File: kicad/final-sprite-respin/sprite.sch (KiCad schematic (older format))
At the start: 69 parts, among them J1 M20-7910442R, U1 CC430F513X, U2 LSM9DS1, U3 SPRITETCXO_TCXO_7Z, U4 DRV8837, U5 ADP5092, U6 DRV8837, U7 DRV8837, U8 TASC, U9 TASC, X1 SPRITEPIN_SPRITE_PIN, X2 SPRITEPIN_SPRITE_PIN

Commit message: Route spiral inductor
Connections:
- net labels added: SPIRAL
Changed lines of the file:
@@
 Wire Wire Line
 	15250 2950 15950 2950
+Text Label 8350 8950 0    50   ~ 0
+SPIRAL
 $EndSCHEMATC

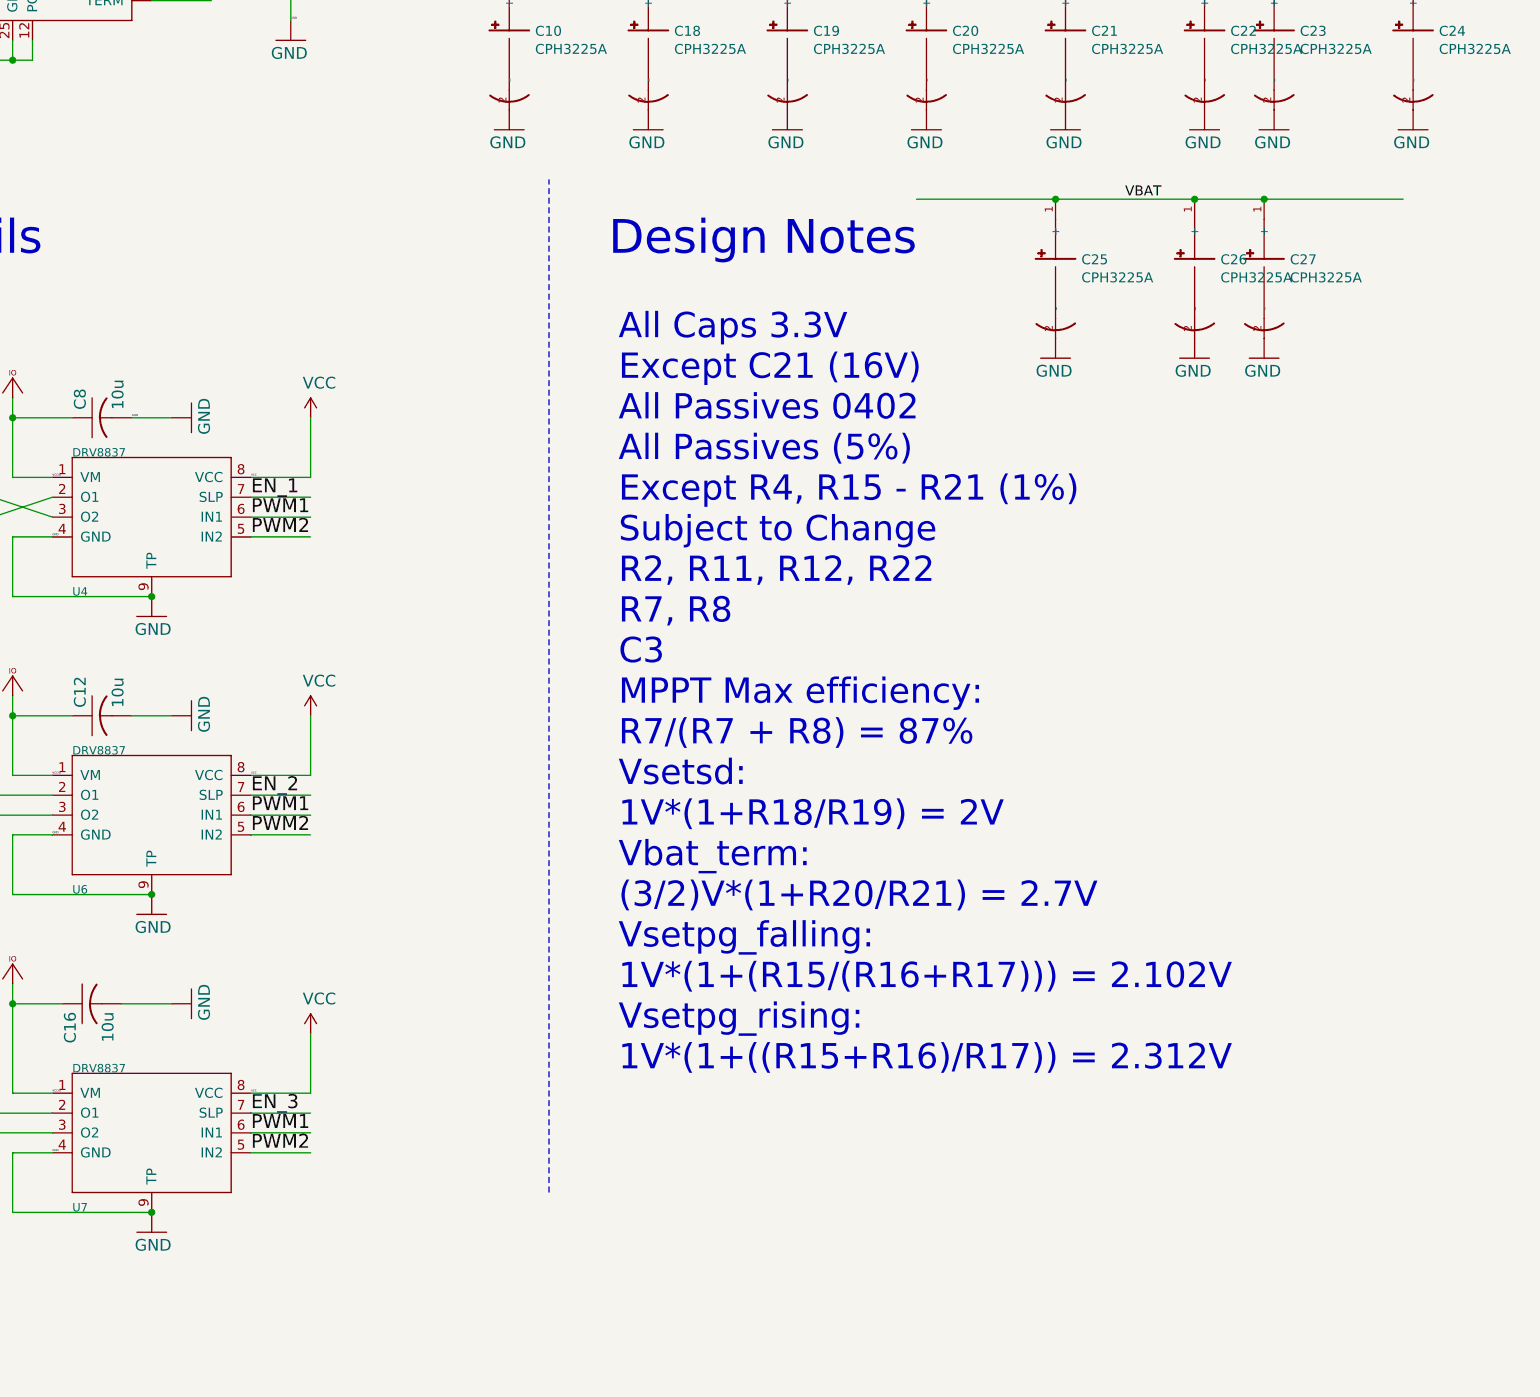
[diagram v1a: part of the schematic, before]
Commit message: updated pcb with spots for 6 more caps
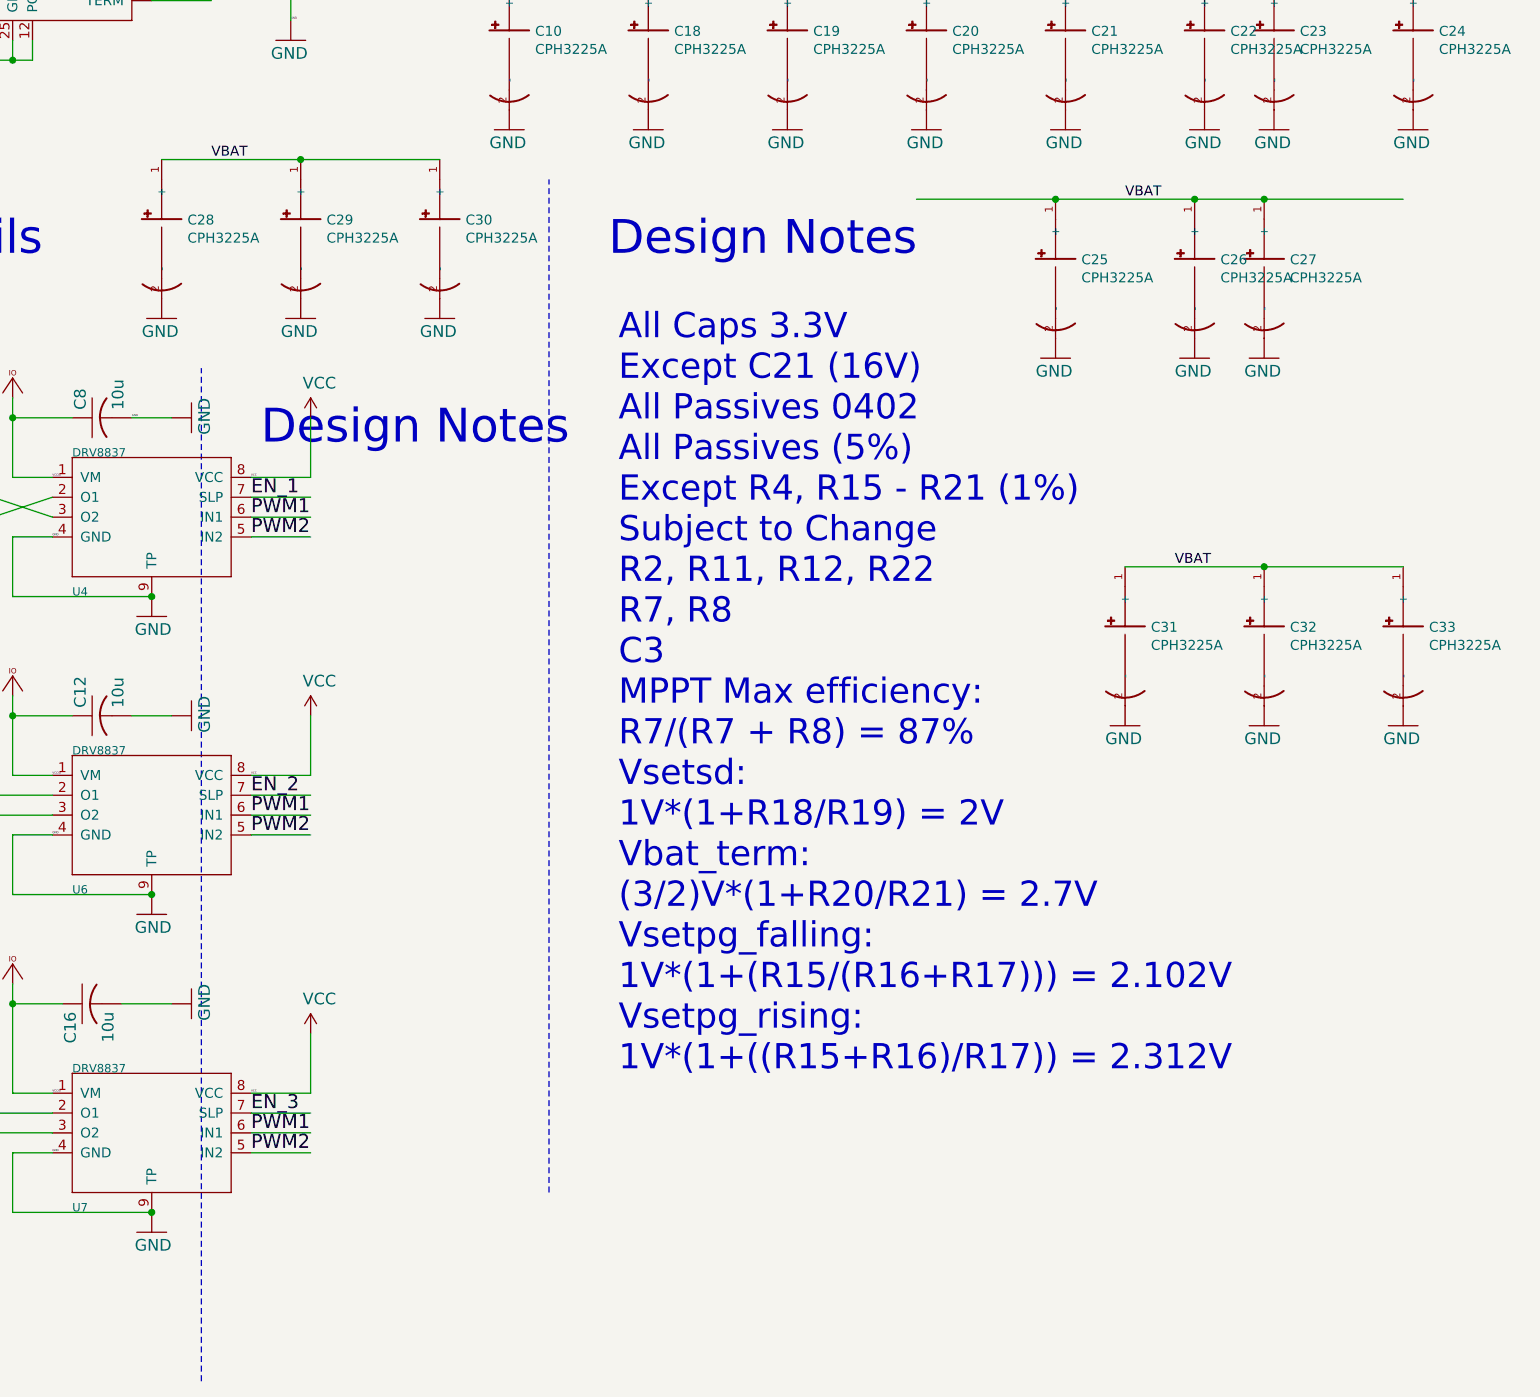
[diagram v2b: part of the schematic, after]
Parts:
- added C28, C29, C30, C31, C32, C33: CPH3225A, sprite:CAPCP3225X100N, symbol sprite-rescue:CPH3225A-CPH3225A
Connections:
- wire segments 272 -> 276
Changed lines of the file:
@@
 Wire Wire Line
 	11700 3500 12400 3500
-Connection ~ 12400 3500
 Wire Wire Line
 	12400 3500 13100 3500
@@
 Wire Wire Line
 	13800 3500 13100 3500
-Connection ~ 13800 3500
-Connection ~ 13100 3500
-Connection ~ 14500 3500
 $Comp
 L sprite-eagle-import:GND #GND0107
@@
 Text Label 8350 8950 0    50   ~ 0
 SPIRAL
+Connection ~ 14500 3500
+Connection ~ 12400 3500
+Connection ~ 13800 3500
+Connection ~ 13100 3500
+Wire Notes Line
+	10150 10600 10150 5500
+Text Notes 10450 5900 0    170  ~ 0
+Design Notes
+$Comp
+L sprite-eagle-import:GND #GND0112
+U 1 0 5BA7FDCD
+P 9950 5250
+F 0 "#GND0112" H 9950 5250 50  0001 C CNN
+F 1 "GND" H 9850 5150 59  0000 L BNN
+F 2 "" H 9950 5250 50  0001 C CNN
+F 3 "" H 9950 5250 50  0001 C CNN
+	1    9950 5250
+	1    0    0    -1
+$EndComp
+$Comp
+L sprite-rescue:CPH3225A-CPH3225A C28
+U 1 1 5BA7FDD8
+P 9950 4750
+F 0 "C28" H 10080 4746 50  0000 L CNN
+F 1 "CPH3225A" H 10080 4655 50  0000 L CNN
+F 2 "sprite:CAPCP3225X100N" H 9950 4750 50  0001 L BNN
+F 3 "Seiko" H 9950 4750 50  0001 L BNN
+F 4 "1210 Seiko" H 9950 4750 50  0001 L BNN "Field4"
+F 5 "https://www.digikey.com/product-detail/en/seiko-instruments/CPH3225A/728-1127-1-ND/8692445?utm_source=snapeda&utm_medium=aggregator&utm_campaign=symbol" H 9950 4750 50  0001 L BNN "Field5"
+F 6 "728-1127-1-ND" H 9950 4750 50  0001 L BNN "Field6"
+F 7 "Cap 11mf 3.3v Surface Mount" H 9950 4750 50  0001 L BNN "Field7"
+F 8 "CPH3225A" H 9950 4750 50  0001 L BNN "Field8"
+	1    9950 4750
+	1    0    0    -1
+$EndComp
+$Comp
+L sprite-eagle-import:GND #GND0113
+U 1 0 5BA7FDDE
+P 10650 5250
+F 0 "#GND0113" H 10650 5250 50  0001 C CNN
+F 1 "GND" H 10550 5150 59  0000 L BNN
+F 2 "" H 10650 5250 50  0001 C CNN
+F 3 "" H 10650 5250 50  0001 C CNN
+	1    10650 5250
+	1    0    0    -1
+$EndComp
+$Comp
+L sprite-rescue:CPH3225A-CPH3225A C29
+U 1 1 5BA7FDE9
+P 10650 4750
+F 0 "C29" H 10780 4746 50  0000 L CNN
+F 1 "CPH3225A" H 10780 4655 50  0000 L CNN
+F 2 "sprite:CAPCP3225X100N" H 10650 4750 50  0001 L BNN
+F 3 "Seiko" H 10650 4750 50  0001 L BNN
+F 4 "1210 Seiko" H 10650 4750 50  0001 L BNN "Field4"
+F 5 "https://www.digikey.com/product-detail/en/seiko-instruments/CPH3225A/728-1127-1-ND/8692445?utm_source=snapeda&utm_medium=aggregator&utm_campaign=symbol" H 10650 4750 50  0001 L BNN "Field5"
+F 6 "728-1127-1-ND" H 10650 4750 50  0001 L BNN "Field6"
+F 7 "Cap 11mf 3.3v Surface Mount" H 10650 4750 50  0001 L BNN "Field7"
+F 8 "CPH3225A" H 10650 4750 50  0001 L BNN "Field8"
+	1    10650 4750
+	1    0    0    -1
+$EndComp
+$Comp
+L sprite-eagle-import:GND #GND0114
+U 1 0 5BA7FDEF
+P 11350 5250
+F 0 "#GND0114" H 11350 5250 50  0001 C CNN
+F 1 "GND" H 11250 5150 59  0000 L BNN
+F 2 "" H 11350 5250 50  0001 C CNN
+F 3 "" H 11350 5250 50  0001 C CNN
+	1    11350 5250
+	1    0    0    -1
+$EndComp
+$Comp
+L sprite-rescue:CPH3225A-CPH3225A C30
+U 1 1 5BA7FDFA
+P 11350 4750
+F 0 "C30" H 11480 4746 50  0000 L CNN
+F 1 "CPH3225A" H 11480 4655 50  0000 L CNN
+F 2 "sprite:CAPCP3225X100N" H 11350 4750 50  0001 L BNN
+F 3 "Seiko" H 11350 4750 50  0001 L BNN
+F 4 "1210 Seiko" H 11350 4750 50  0001 L BNN "Field4"
+F 5 "https://www.digikey.com/product-detail/en/seiko-instruments/CPH3225A/728-1127-1-ND/8692445?utm_source=snapeda&utm_medium=aggregator&utm_campaign=symbol" H 11350 4750 50  0001 L BNN "Field5"
+F 6 "728-1127-1-ND" H 11350 4750 50  0001 L BNN "Field6"
+F 7 "Cap 11mf 3.3v Surface Mount" H 11350 4750 50  0001 L BNN "Field7"
+F 8 "CPH3225A" H 11350 4750 50  0001 L BNN "Field8"
+	1    11350 4750
+	1    0    0    -1
+$EndComp
+Wire Wire Line
+	9950 4450 10650 4450
+Wire Wire Line
+	10650 4450 11350 4450
+Text Label 10200 4450 0    50   ~ 0
+VBAT
+Connection ~ 10650 4450
+$Comp
+L sprite-eagle-import:GND #GND0115
+U 1 0 5BABD0FA
+P 14800 7300
+F 0 "#GND0115" H 14800 7300 50  0001 C CNN
+F 1 "GND" H 14700 7200 59  0000 L BNN
+F 2 "" H 14800 7300 50  0001 C CNN
+F 3 "" H 14800 7300 50  0001 C CNN
+	1    14800 7300
+	1    0    0    -1
+$EndComp
+$Comp
+L sprite-rescue:CPH3225A-CPH3225A C31
+U 1 1 5BABD105
+P 14800 6800
+F 0 "C31" H 14930 6796 50  0000 L CNN
+F 1 "CPH3225A" H 14930 6705 50  0000 L CNN
+F 2 "sprite:CAPCP3225X100N" H 14800 6800 50  0001 L BNN
+F 3 "Seiko" H 14800 6800 50  0001 L BNN
+F 4 "1210 Seiko" H 14800 6800 50  0001 L BNN "Field4"
+F 5 "https://www.digikey.com/product-detail/en/seiko-instruments/CPH3225A/728-1127-1-ND/8692445?utm_source=snapeda&utm_medium=aggregator&utm_campaign=symbol" H 14800 6800 50  0001 L BNN "Field5"
+F 6 "728-1127-1-ND" H 14800 6800 50  0001 L BNN "Field6"
+F 7 "Cap 11mf 3.3v Surface Mount" H 14800 6800 50  0001 L BNN "Field7"
+F 8 "CPH3225A" H 14800 6800 50  0001 L BNN "Field8"
+	1    14800 6800
+	1    0    0    -1
+$EndComp
+$Comp
+L sprite-eagle-import:GND #GND0116
+U 1 0 5BABD10B
+P 15500 7300
+F 0 "#GND0116" H 15500 7300 50  0001 C CNN
+F 1 "GND" H 15400 7200 59  0000 L BNN
+F 2 "" H 15500 7300 50  0001 C CNN
+F 3 "" H 15500 7300 50  0001 C CNN
+	1    15500 7300
+	1    0    0    -1
+$EndComp
+$Comp
+L sprite-rescue:CPH3225A-CPH3225A C32
+U 1 1 5BABD116
+P 15500 6800
+F 0 "C32" H 15630 6796 50  0000 L CNN
+F 1 "CPH3225A" H 15630 6705 50  0000 L CNN
+F 2 "sprite:CAPCP3225X100N" H 15500 6800 50  0001 L BNN
+F 3 "Seiko" H 15500 6800 50  0001 L BNN
+F 4 "1210 Seiko" H 15500 6800 50  0001 L BNN "Field4"
+F 5 "https://www.digikey.com/product-detail/en/seiko-instruments/CPH3225A/728-1127-1-ND/8692445?utm_source=snapeda&utm_medium=aggregator&utm_campaign=symbol" H 15500 6800 50  0001 L BNN "Field5"
+F 6 "728-1127-1-ND" H 15500 6800 50  0001 L BNN "Field6"
+F 7 "Cap 11mf 3.3v Surface Mount" H 15500 6800 50  0001 L BNN "Field7"
+F 8 "CPH3225A" H 15500 6800 50  0001 L BNN "Field8"
+	1    15500 6800
+	1    0    0    -1
+$EndComp
+$Comp
+L sprite-eagle-import:GND #GND0117
+U 1 0 5BABD11C
+P 16200 7300
+F 0 "#GND0117" H 16200 7300 50  0001 C CNN
+F 1 "GND" H 16100 7200 59  0000 L BNN
+F 2 "" H 16200 7300 50  0001 C CNN
+F 3 "" H 16200 7300 50  0001 C CNN
+	1    16200 7300
+	1    0    0    -1
+$EndComp
+$Comp
+L sprite-rescue:CPH3225A-CPH3225A C33
+U 1 1 5BABD127
+P 16200 6800
+F 0 "C33" H 16330 6796 50  0000 L CNN
+F 1 "CPH3225A" H 16330 6705 50  0000 L CNN
+F 2 "sprite:CAPCP3225X100N" H 16200 6800 50  0001 L BNN
+F 3 "Seiko" H 16200 6800 50  0001 L BNN
+F 4 "1210 Seiko" H 16200 6800 50  0001 L BNN "Field4"
+F 5 "https://www.digikey.com/product-detail/en/seiko-instruments/CPH3225A/728-1127-1-ND/8692445?utm_source=snapeda&utm_medium=aggregator&utm_campaign=symbol" H 16200 6800 50  0001 L BNN "Field5"
+F 6 "728-1127-1-ND" H 16200 6800 50  0001 L BNN "Field6"
+F 7 "Cap 11mf 3.3v Surface Mount" H 16200 6800 50  0001 L BNN "Field7"
+F 8 "CPH3225A" H 16200 6800 50  0001 L BNN "Field8"
+	1    16200 6800
+	1    0    0    -1
+$EndComp
+Wire Wire Line
+	14800 6500 15500 6500
+Wire Wire Line
+	15500 6500 16200 6500
+Text Label 15050 6500 0    50   ~ 0
+VBAT
+Connection ~ 15500 6500
 $EndSCHEMATC
